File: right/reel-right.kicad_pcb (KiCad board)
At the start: 2 copper layers, 6.1 x 13.9 mm, 44 parts, among them J1 Conn_01x02, SW1 SW_Push, SW10 SW_Push, SW11 SW_Push, SW12 SW_Push, SW13 SW_Push, SW14 SW_Push, SW15 SW_Push, SW16 SW_Push, SW17 SW_Push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

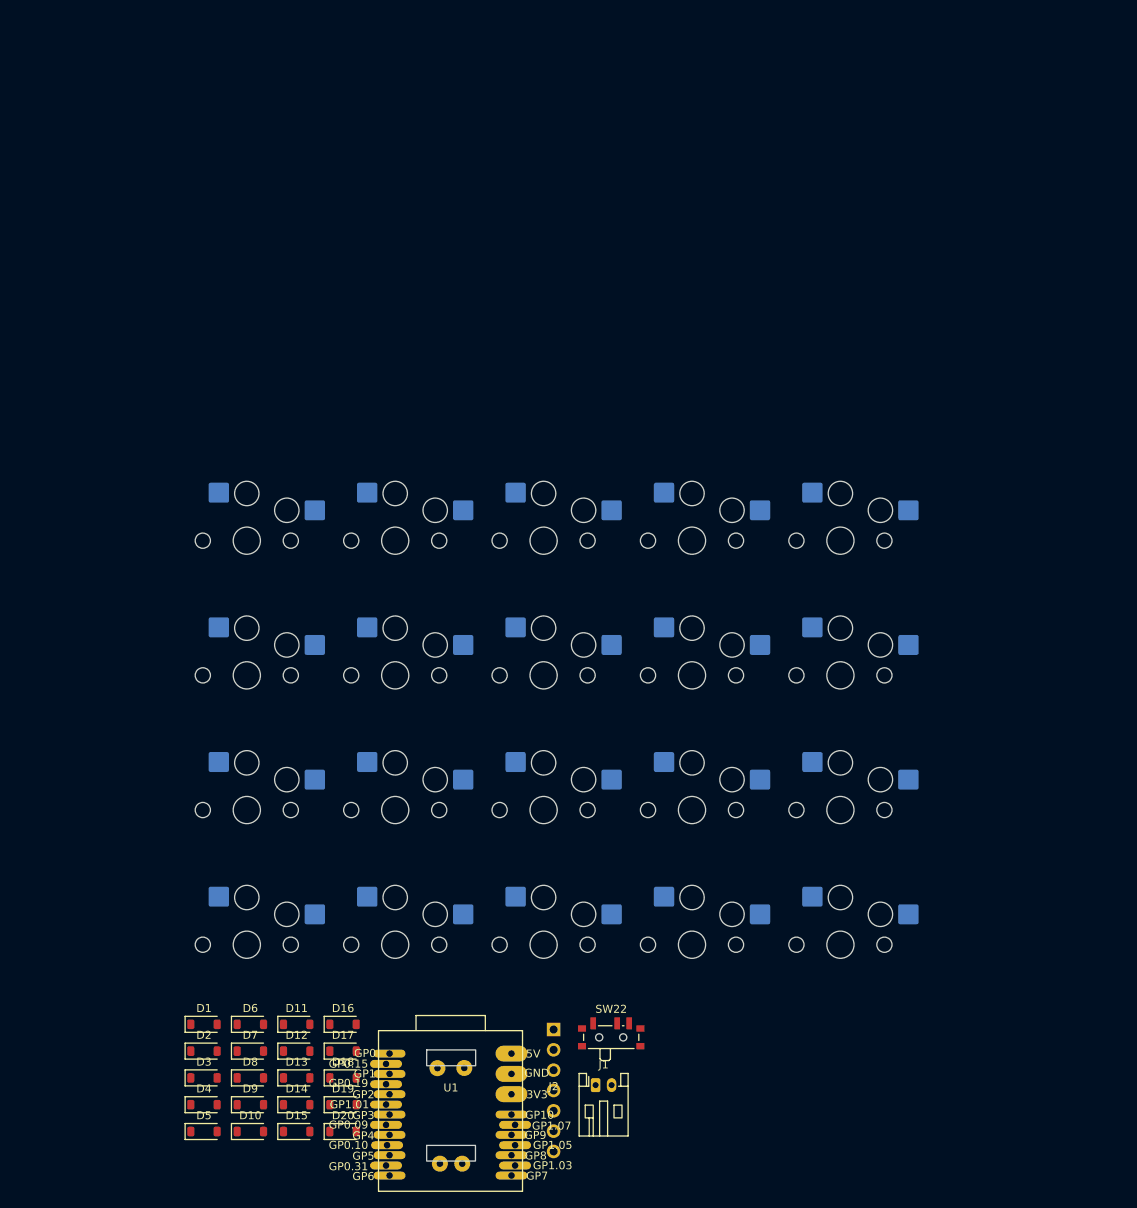
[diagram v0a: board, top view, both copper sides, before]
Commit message: Update left and right PCB layouts
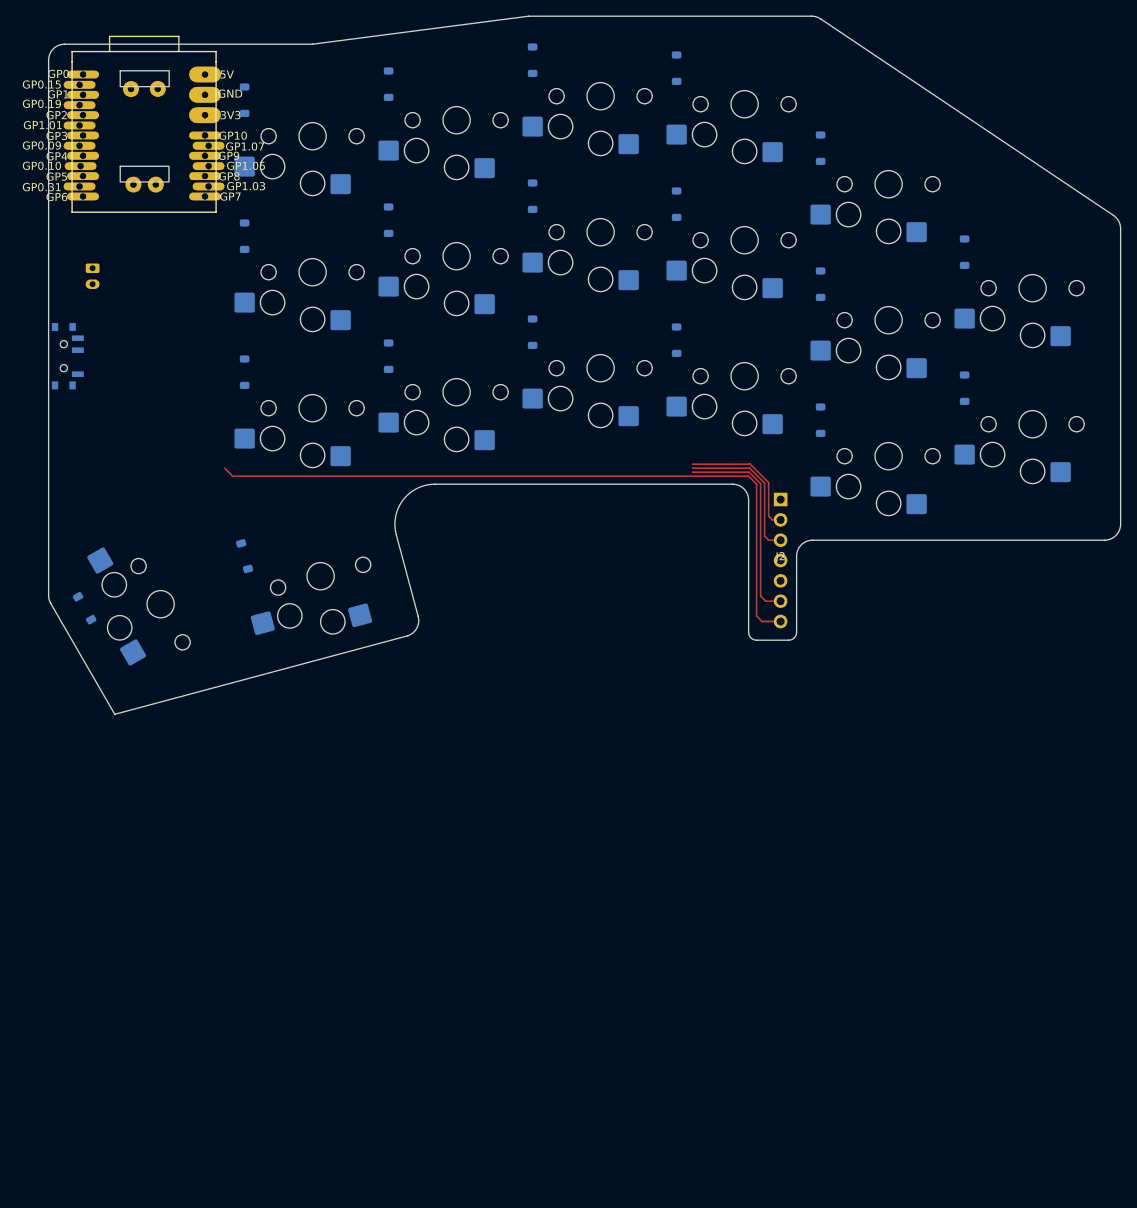
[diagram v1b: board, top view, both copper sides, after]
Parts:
- removed D20: D, Diode_SMD:D_SOD-123
- removed SW20: SW_Push, reel:SW_Hotswap_Kailh_Choc_V1_1.00u-NoClickHole
- D1, D10, D11, D12, D13, D14, D15, D16, D17, D18, D19, D2, D3, D4, D5, D6, D7, D8, D9, J1, SW22: moved to B.Cu
- moved D2 136.3 mm to (125.5, 52.0), turned to -90 degrees
- moved D1 133.9 mm to (143.5, 62.0), turned to -90 degrees
- moved D3 133.7 mm to (107.5, 51.0), turned to -90 degrees
- moved D4 129.6 mm to (89.5, 54.0), turned to -90 degrees
- moved D5 129.0 mm to (71.5, 56.0), turned to -90 degrees
- moved U1 128.2 mm to (59.0, 57.0)
- moved D16 123.9 mm to (161.5, 75.0), turned to -90 degrees
- moved J1 119.9 mm to (52.5, 77.0), turned to -90 degrees
- moved D7 118.5 mm to (125.5, 69.0), turned to -90 degrees
- moved D6 116.8 mm to (143.5, 79.0), turned to -90 degrees
- moved D8 115.7 mm to (107.5, 68.0), turned to -90 degrees
- moved D17 113.6 mm to (161.5, 92.0), turned to -90 degrees
- moved D10 111.9 mm to (71.5, 73.0), turned to -90 degrees
- moved D9 111.9 mm to (89.5, 71.0), turned to -90 degrees
- moved SW22 108.8 mm to (49.2, 88.0), turned to 90 degrees
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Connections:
- SW22 pad 1: unconnected-(SW22-A-Pad1) -> VBAT_SW
- SW22 pad 3: VBAT_SW -> unconnected-(SW22-C-Pad3)
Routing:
- net MOTION: track 0.00 -> 87.1 mm
- net SDIO: track 0.00 -> 25.9 mm
- net GND: track 0.00 -> 18.6 mm
- net nCS: track 0.00 -> 16.5 mm
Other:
- board size 6.1 x 13.9 mm -> 134 x 87.3 mm

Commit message: Update right PCB layout
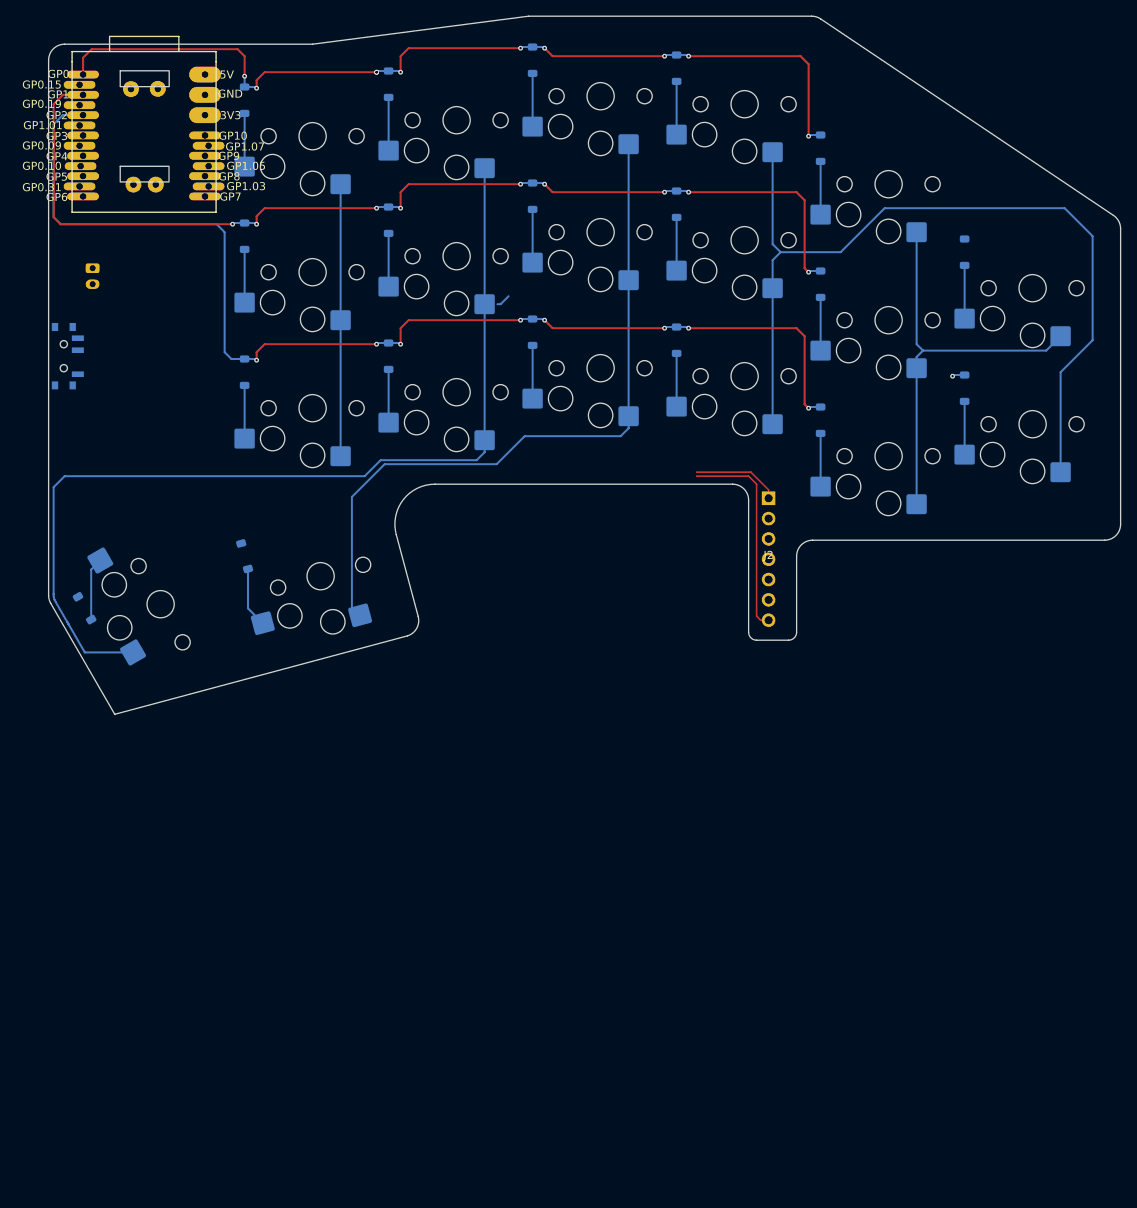
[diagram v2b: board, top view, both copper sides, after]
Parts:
- moved J2 1.51 mm to (137.0, 113.4)
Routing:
- net Row2: track 0.00 -> 141.6 mm, vias 0 -> 8
- net Row1: track 0.00 -> 128.5 mm, vias 0 -> 9
- net Col3: track 0.00 -> 119.3 mm
- net Row0: track 0.00 -> 113.1 mm, vias 0 -> 10
- net Col1: track 0.00 -> 108.7 mm
- net Col2: track 0.00 -> 89.3 mm
- net MOTION: track 87.1 -> 26.1 mm
- net Col0: track 0.00 -> 52.6 mm
- net Col4: track 0.00 -> 34.0 mm
- net SDIO: track 25.9 -> 0.00 mm
- net GND: track 18.6 -> 0.00 mm
- net nCS: track 16.5 -> 0.00 mm
- net SCLK: track 0.00 -> 11.0 mm
- net Net-(D19-A): track 0.00 -> 7.86 mm
- net Net-(D18-A): track 0.00 -> 7.54 mm
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
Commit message: Update left and right board assets
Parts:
- moved J2 4.39 mm to (136.6, 117.8)
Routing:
- net MOTION: track 26.1 -> 0.00 mm
- net SCLK: track 11.0 -> 0.00 mm
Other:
- outline, holes or cut-outs redrawn
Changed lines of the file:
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@@
 	(generator_version "10.0")
 	(general
-		(thickness 1.6)
+		(thickness 1.09)
 		(legacy_teardrops no)
 	)
@@
 	)
 	(setup
+		(stackup
+			(layer "F.SilkS"
+				(type "Top Silk Screen")
+			)
+			(layer "F.Paste"
+				(type "Top Solder Paste")
+			)
+			(layer "F.Mask"
+				(type "Top Solder Mask")
+				(thickness 0.01)
+			)
+			(layer "F.Cu"
+				(type "copper")
+				(thickness 0.035)
+			)
+			(layer "dielectric 1"
+				(type "core")
+				(thickness 1)
+				(material "FR4")
+				(epsilon_r 4.5)
+				(loss_tangent 0.02)
+			)
+			(layer "B.Cu"
+				(type "copper")
+				(thickness 0.035)
+			)
+			(layer "B.Mask"
+				(type "Bottom Solder Mask")
+				(thickness 0.01)
+			)
+			(layer "B.Paste"
+				(type "Bottom Solder Paste")
+			)
+			(layer "B.SilkS"
+				(type "Bottom Silk Screen")
+			)
+			(copper_finish "None")
+			(dielectric_constraints no)
+		)
 		(pad_to_mask_clearance 0)
 		(allow_soldermask_bridges_in_footprints no)
@@
 		(capping no)
 		(filling no)
+		(zone_defaults)
 		(pcbplotparams
 			(layerselection 0x00000000_00000000_55555555_5755f5ff)
@@
 	(footprint "reel:pmw3610_connector"
 		(layer "F.Cu")
-		(at 137 113.38)
+		(at 136.6 117.75)
 		(property "Reference" "J2"
 			(at 0 -0.5 0)
@@
 	)
 	(gr_line
-		(start 132.5 104)
+		(start 134.075 104)
 		(end 95.284076 104)
 		(stroke
@@
 		(layer "Edge.Cuts")
 	)
-	(gr_arc
-		(start 132.5 104)
-		(mid 133.914214 104.585786)
-		(end 134.5 106)
-		(stroke
-			(width 0.05)
-			(type default)
-		)
-		(layer "Edge.Cuts")
-	)
 	(gr_line
-		(start 134.5 122.5)
-		(end 134.5 106)
-		(stroke
-			(width 0.05)
-			(type default)
-		)
-		(layer "Edge.Cuts")
-	)
-	(gr_arc
-		(start 135.5 123.5)
-		(mid 134.792893 123.207107)
-		(end 134.5 122.5)
+		(start 134.075 128)
+		(end 134.075 104)
 		(stroke
 			(width 0.05)
-			(type default)
+			(type solid)
 		)
 		(layer "Edge.Cuts")
 	)
 	(gr_line
-		(start 135.5 123.5)
-		(end 139.5 123.5)
+		(start 134.075 128)
+		(end 140.5 128)
 		(stroke
 			(width 0.05)
@@
 		(layer "Edge.Cuts")
 	)
-	(gr_arc
-		(start 140.5 122.5)
-		(mid 140.207107 123.207107)
-		(end 139.5 123.5)
-		(stroke
-			(width 0.05)
-			(type default)
-		)
-		(layer "Edge.Cuts")
-	)
 	(gr_line
-		(start 140.5 122.5)
+		(start 140.5 128)
 		(end 140.5 113)
 		(stroke
@@
 	)
 	(segment
-		(start 134.79 102.5)
-		(end 128 102.5)
-		(width 0.2)
-		(layer "F.Cu")
-		(net "SCLK")
-	)
-	(segment
-		(start 137 105.76)
-		(end 137 104.71)
-		(width 0.2)
-		(layer "F.Cu")
-		(net "SCLK")
-	)
-	(segment
-		(start 137 104.71)
-		(end 134.79 102.5)
-		(width 0.2)
-		(layer "F.Cu")
-		(net "SCLK")
-	)
-	(segment
-		(start 136 121)
-		(end 135.5 120.5)
-		(width 0.2)
-		(layer "F.Cu")
-		(net "MOTION")
-	)
-	(segment
-		(start 137 121)
-		(end 136 121)
-		(width 0.2)
-		(layer "F.Cu")
-		(net "MOTION")
-	)
-	(segment
-		(start 135.5 120.5)
-		(end 135.5 104)
-		(width 0.2)
-		(layer "F.Cu")
-		(net "MOTION")
-	)
-	(segment
-		(start 134.5 103)
-		(end 128 103)
-		(width 0.2)
-		(layer "F.Cu")
-		(net "MOTION")
-	)
-	(segment
-		(start 135.5 104)
-		(end 134.5 103)
-		(width 0.2)
-		(layer "F.Cu")
-		(net "MOTION")
-	)
-	(segment
